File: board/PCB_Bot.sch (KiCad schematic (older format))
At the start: 5 parts, among them U1 TB6612FNG, U2 LSM9DS1

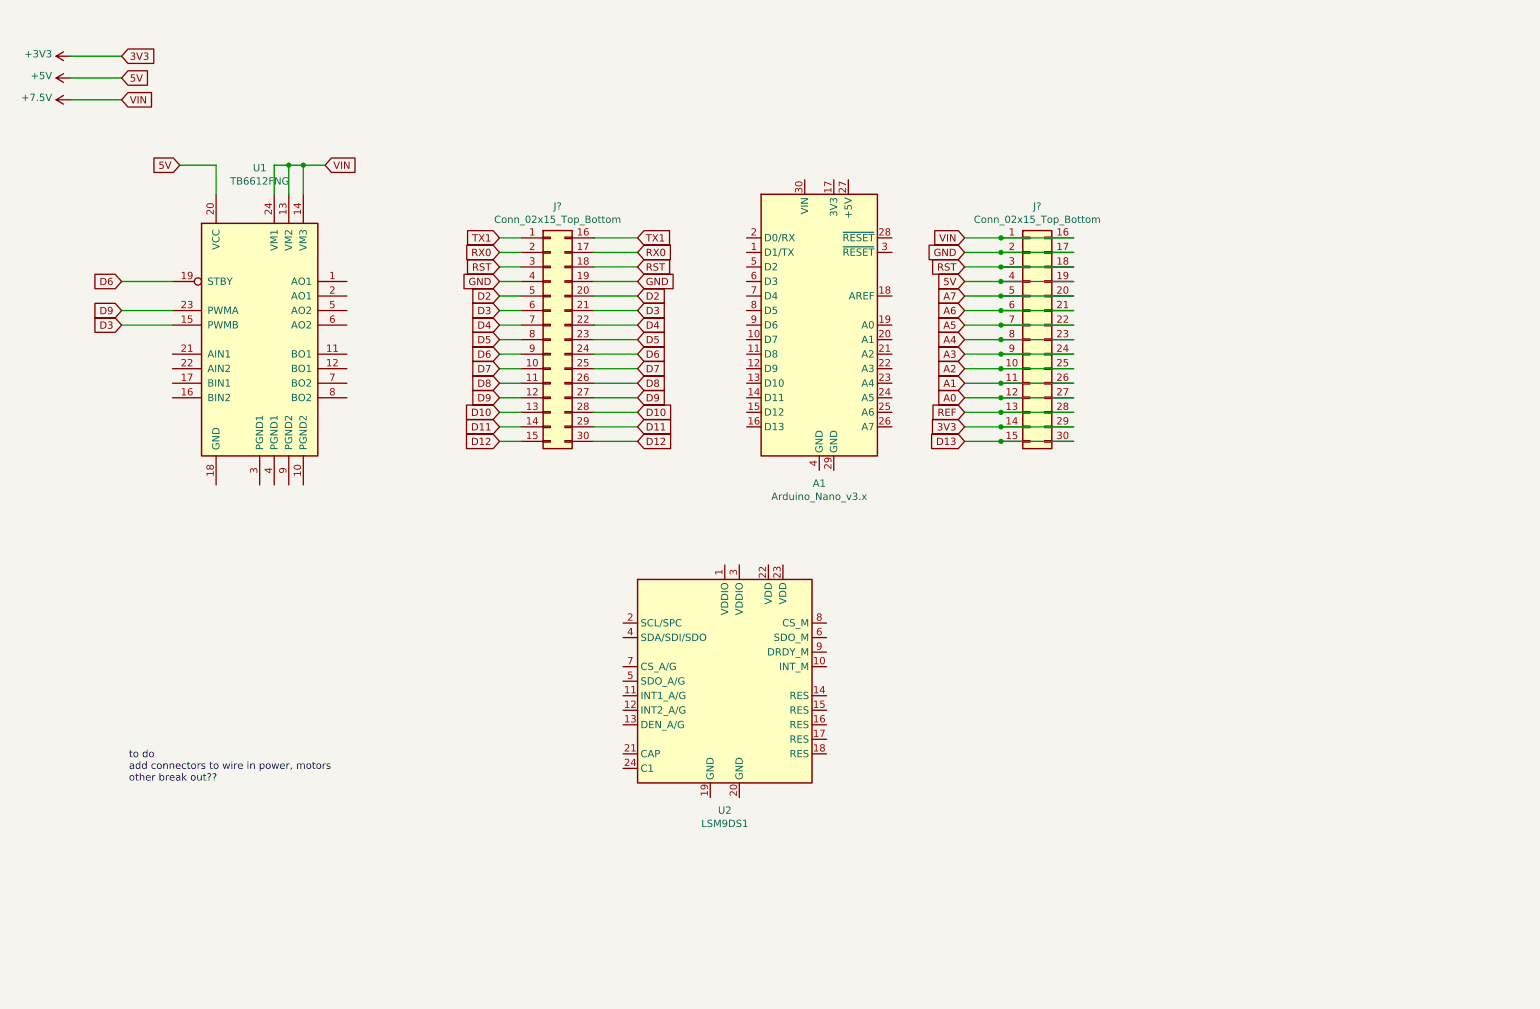
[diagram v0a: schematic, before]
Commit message: update schematic, add 9Dof pdf
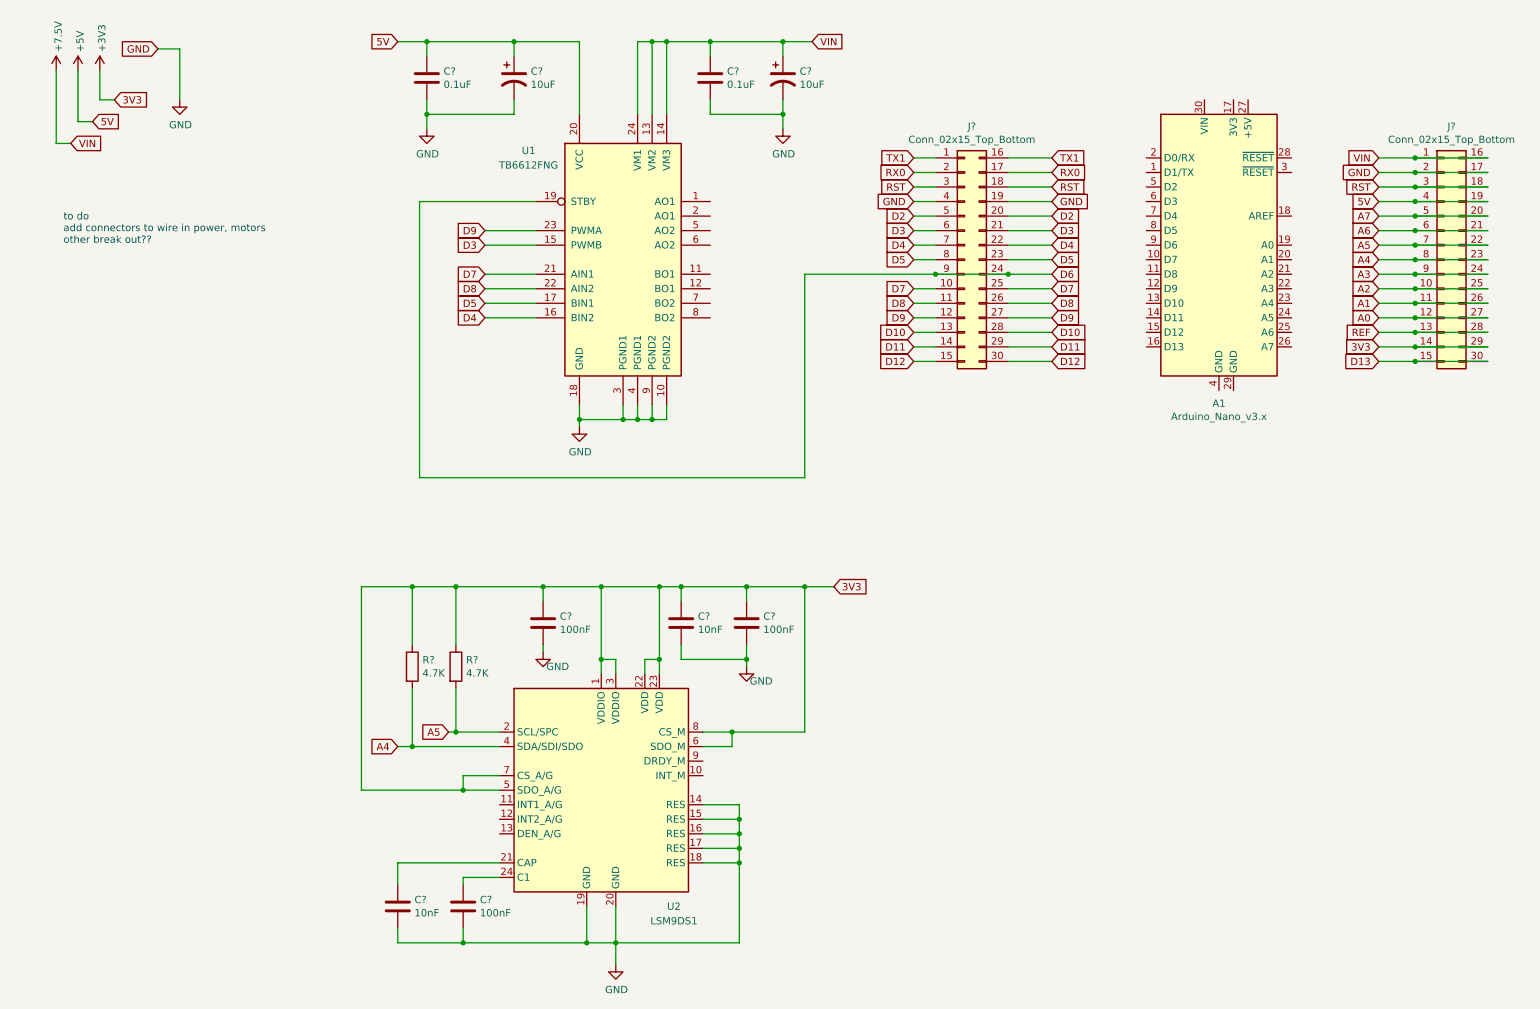
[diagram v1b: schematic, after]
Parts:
- added C? (x2): 0.1uF, symbol Device:C
- added C? (x2): 10uF, symbol Device:CP1
- added C? (x3): 100nF, symbol Device:C
- added C? (x2): 10nF, symbol Device:C
- added R? (x2): 4.7K, symbol Device:R
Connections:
- net +3V3: now also U2.1 (VDDIO), U2.22 (VDD), U2.23 (VDD), U2.3 (VDDIO), U2.5 (SDO_A/G), U2.6 (SDO_M), U2.7 (CS_A/G), U2.8 (CS_M), C?.1, C?.1, C?.1, R?.1, R?.1
- net +5V: now also C?.1, C?.1
- net +7.5V: now also C?.1, C?.1
- net A4: now also U2.4 (SDA/SDI/SDO), R?.2
- net A5: now also U2.2 (SCL/SPC), R?.2
- net D4: now also U1.16 (BIN2)
- net D5: now also U1.17 (BIN1)
- net D7: now also U1.21 (AIN1)
- net D8: now also U1.22 (AIN2)
- net GND: now also U1.10 (PGND2), U1.18 (GND), U1.3 (PGND1), U1.4 (PGND1), U1.9 (PGND2), U2.14 (RES), U2.15 (RES), U2.16 (RES), U2.17 (RES), U2.18 (RES), U2.19 (GND), U2.20 (GND), C?.2, C?.2, C?.2, C?.2, C?.2, C?.2, C?.2, C?.2, C?.2
- net at U2.21 (CAP): now also C?.1
- net at U2.24 (C1): now also C?.1
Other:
- moved on the sheet: A1, J?, U1, U2

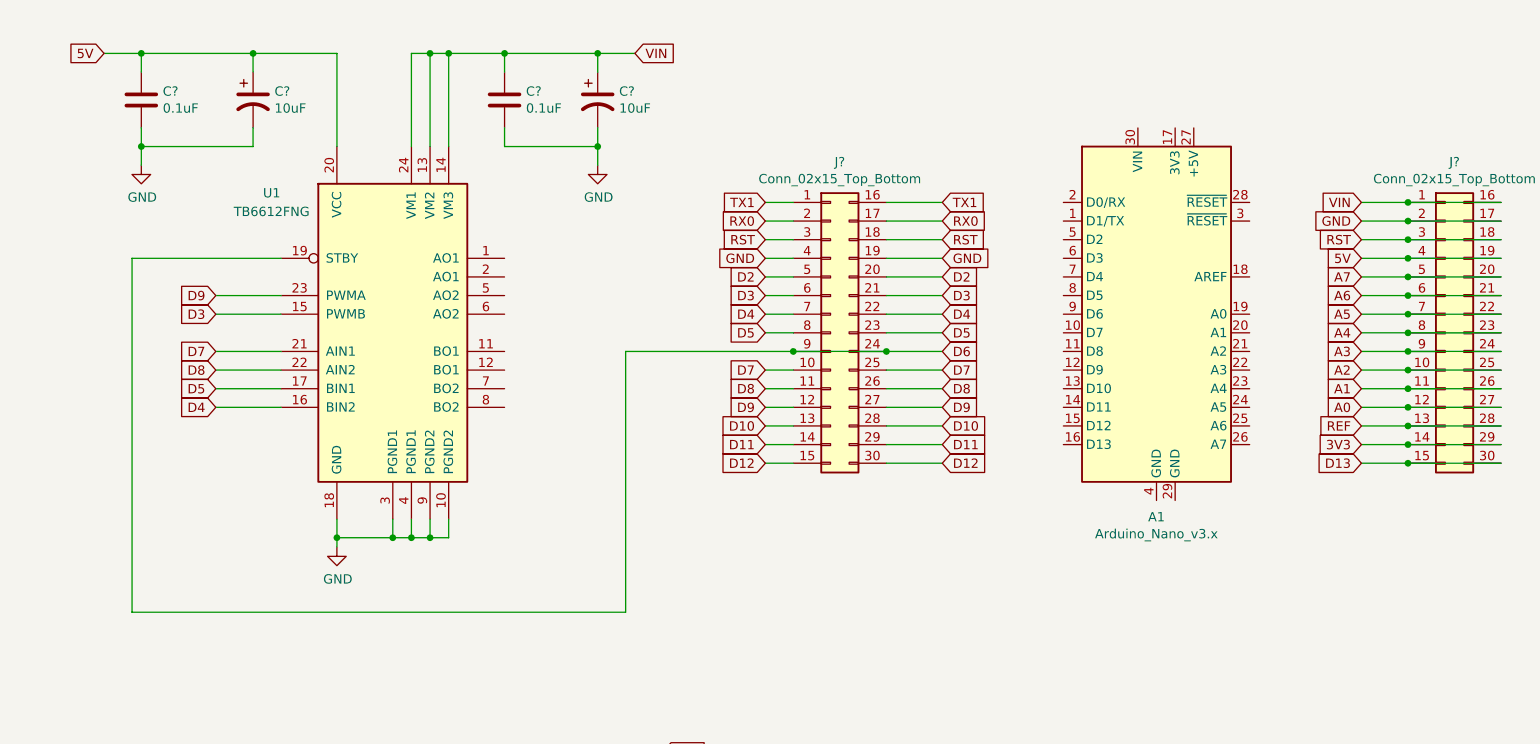
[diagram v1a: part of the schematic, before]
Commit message: add screw terminal to breakout motors and battery input power
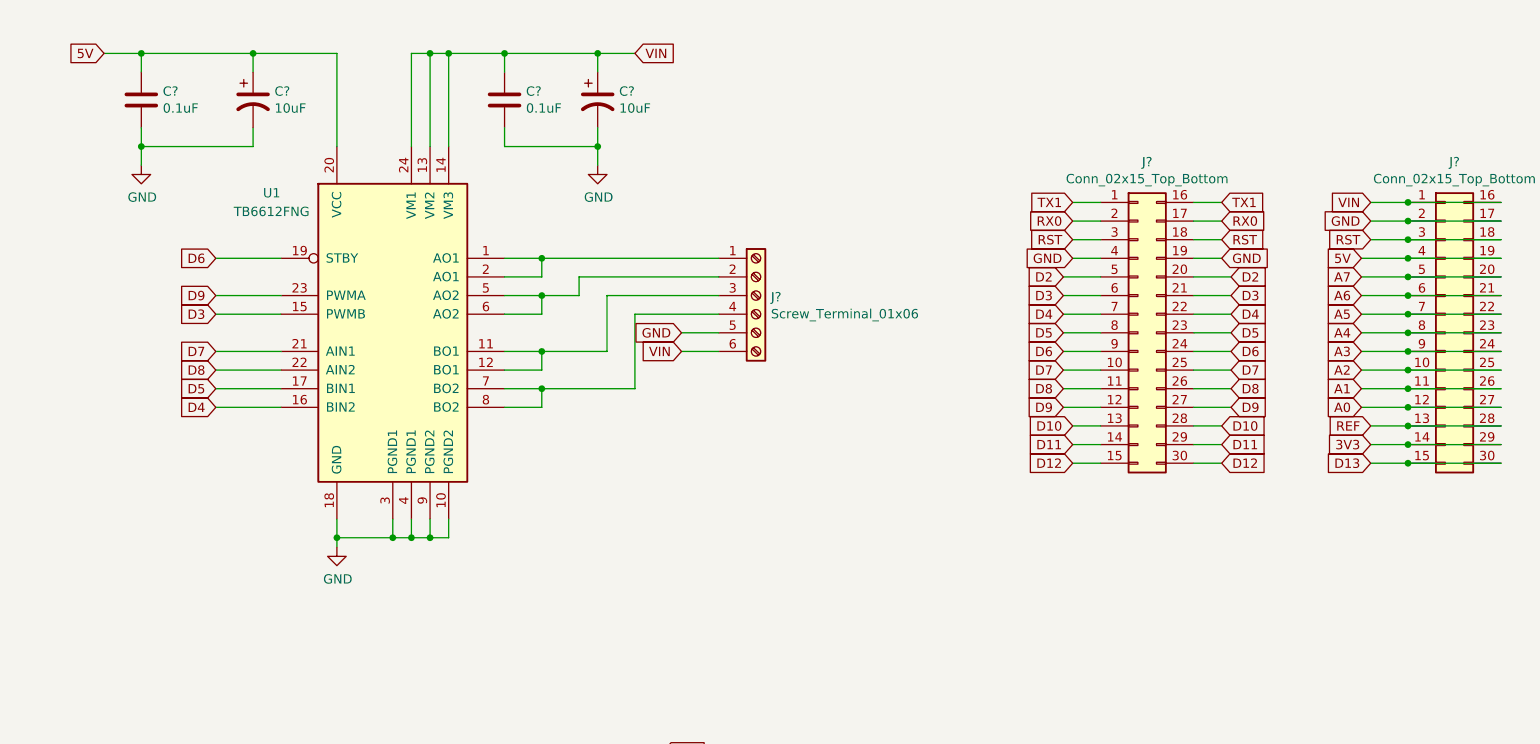
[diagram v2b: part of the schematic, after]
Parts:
- removed A1: Arduino_Nano_v3.x, Module:Arduino_Nano, symbol MCU_Module:Arduino_Nano_v3.x
- added J?: Screw_Terminal_01x06, symbol Connector:Screw_Terminal_01x06
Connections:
- net +7.5V: now also J?.6 (Pin_6)
- net GND: now also J?.5 (Pin_5)
- net at U1.1 (AO1): now also U1.2 (AO1), J?.1 (Pin_1)
- net at U1.11 (BO1): now also U1.12 (BO1), J?.3 (Pin_3)
- net at U1.5 (AO2): now also U1.6 (AO2), J?.2 (Pin_2)
- net at U1.7 (BO2): now also U1.8 (BO2), J?.4 (Pin_4)
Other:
- moved on the sheet: J?

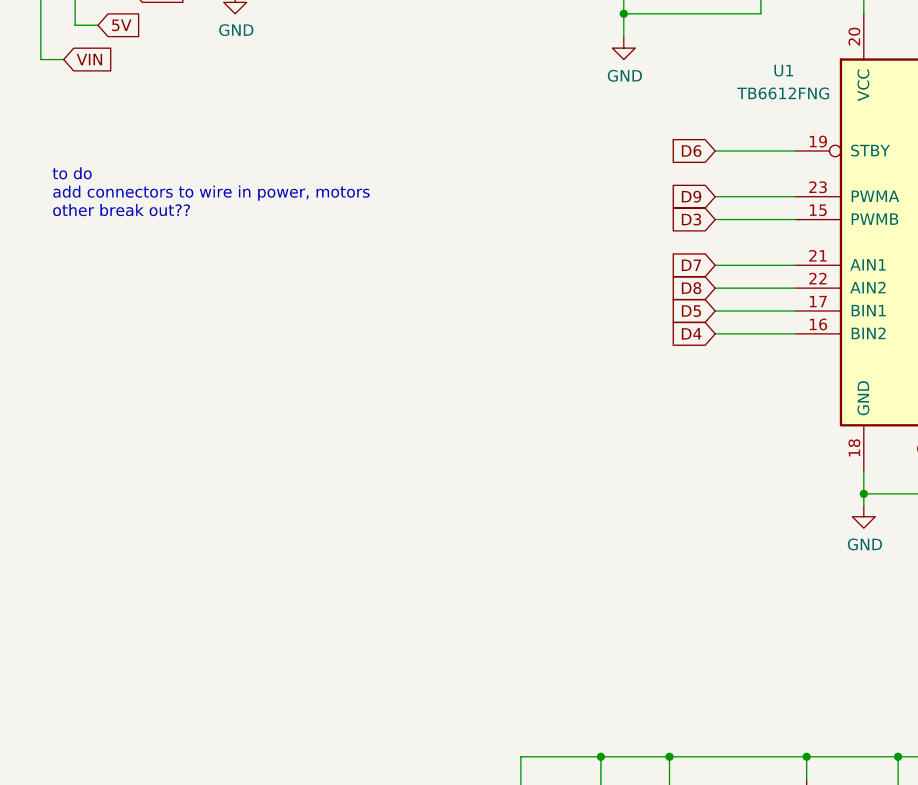
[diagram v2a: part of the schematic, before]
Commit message: add farad values and update schematic
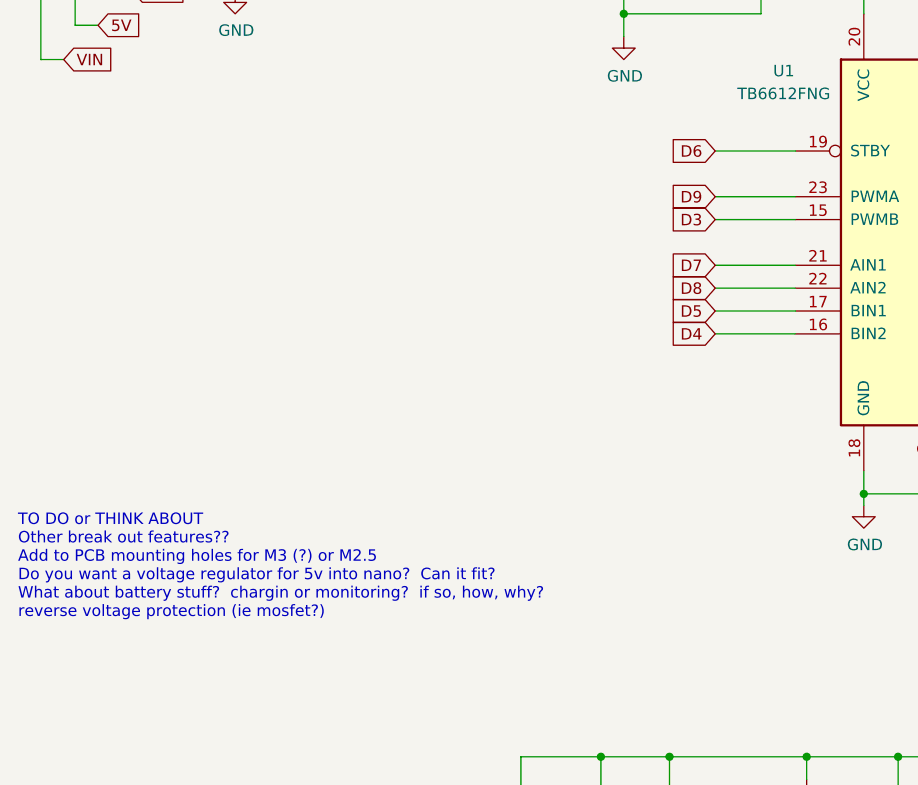
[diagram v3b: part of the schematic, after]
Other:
- note added: "TO DO or THINK ABOUT\nOther break out features??\nAdd to PCB mounting holes for M3 (?) or M2.5\nDo you want a voltage regulator for 5v into nano? Can it fit?\nWhat about battery stuff? chargin or monitoring? if so, how, why?\nreverse voltage protection (ie mosfet?)"
- note removed: "to do\nadd connectors to wire in power, motors\nother break out??"
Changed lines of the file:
@@
 Text GLabel 1150 1150 2    50   Input ~ 0
 3V3
-Text Notes 800  2150 0    50   ~ 0
-to do\nadd connectors to wire in power, motors\nother break out??
+Text Notes 650  3900 0    50   ~ 0
+TO DO or THINK ABOUT\nOther break out features??\nAdd to PCB mounting holes for M3 (?) or M2.5\nDo you want a voltage regulator for 5v into nano?  Can it fit?\nWhat about battery stuff?  chargin or monitoring?  if so, how, why?\nreverse voltage protection (ie mosfet?)
 $Comp
 L power:+7.5V #PWR?
@@
 	3200 4500 3500 4500
 $Bitmap
-Pos 1800 2700
+Pos 3100 7300
 Scale 1.000000
 Data
